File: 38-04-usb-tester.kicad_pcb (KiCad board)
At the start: 2 copper layers, 90 x 90 mm, 68 parts, among them J1 Conn_1x05, J2 USB_C_12401832E402A, J3 USB_C_12401832E402A, J4 USB_Micro-B_KH-MICRO5P-JN, J5 USB_Mini-B_U-M-M5DD-W-1, J6 USB3_A_HC-USB3.0-L168-WP, SW1 SW_DPDT_x2, SW2 ZX-1.27BM-4PSMD, U1 STM32C031K6Tx

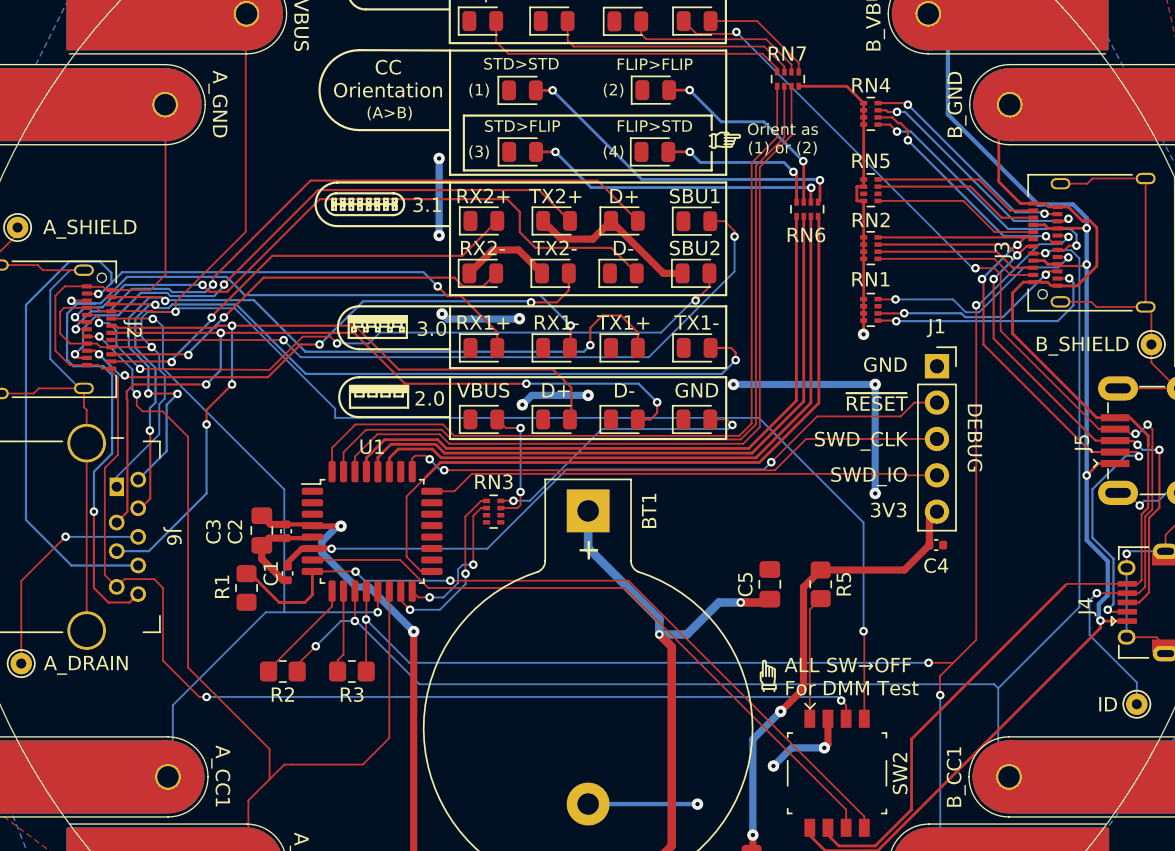
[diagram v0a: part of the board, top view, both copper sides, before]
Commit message: edited schematic, added solder mask expansion, added more thermal reliefs
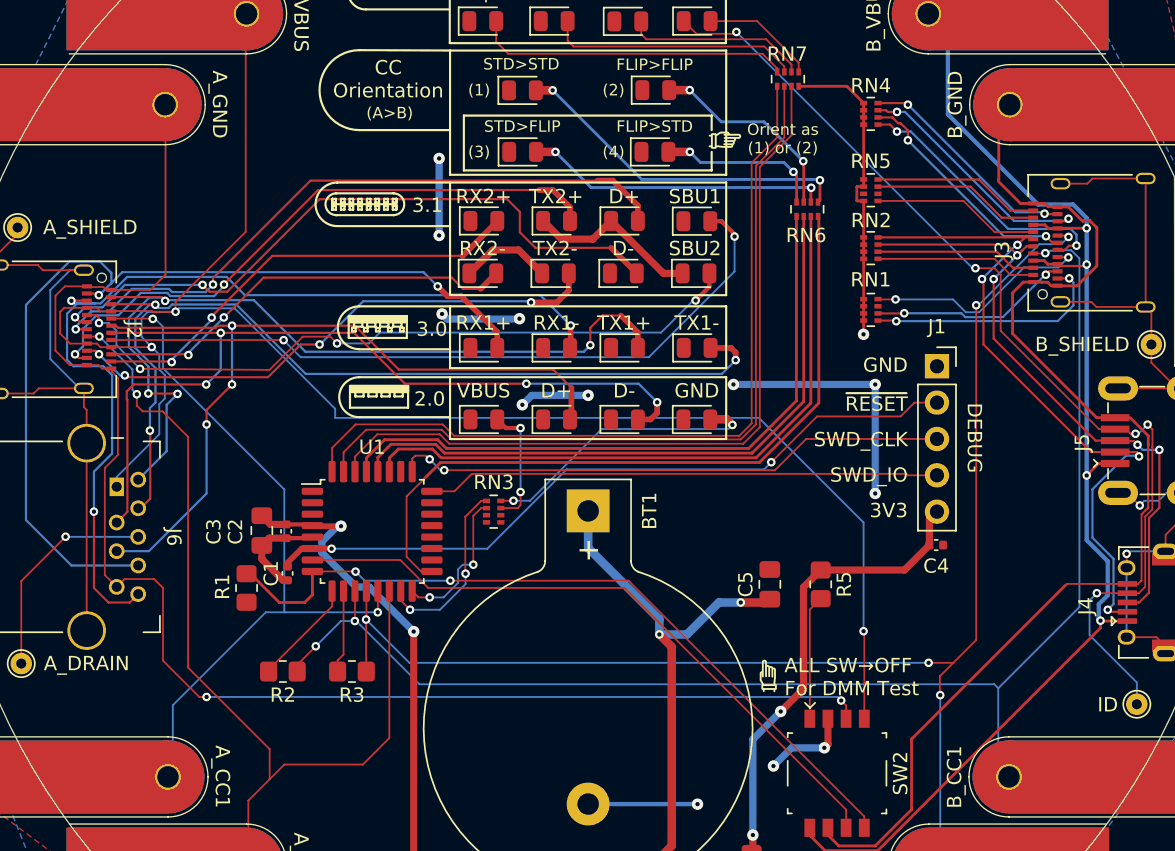
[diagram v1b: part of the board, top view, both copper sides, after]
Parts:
- U1: value STM32C031K6Tx -> STM32C031K6T6
- renumbered REF** to ?
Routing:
- net /A_D2+: track 46.1 -> 46.7 mm
- net /A_SSTx2+: track 42.1 -> 42.7 mm
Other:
- rule pad_to_mask_clearance: 0 -> 0.038
- rule solder_mask_min_width: 0.12 -> 0.1

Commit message: rev 1 sent for prod
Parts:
- R4: value 1K -> 2K
- RN1, RN2, RN3, RN4, RN5, RN6, RN7: value 1K -> 1K6
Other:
- board text added: "Do NOT plug into an external USB port"
- board text added: "ON"
- board text added: "USB Sleuth Rev 1"
- board text removed: "TODO - LOGO"
- board text removed: "USB Sleuth v0.1"

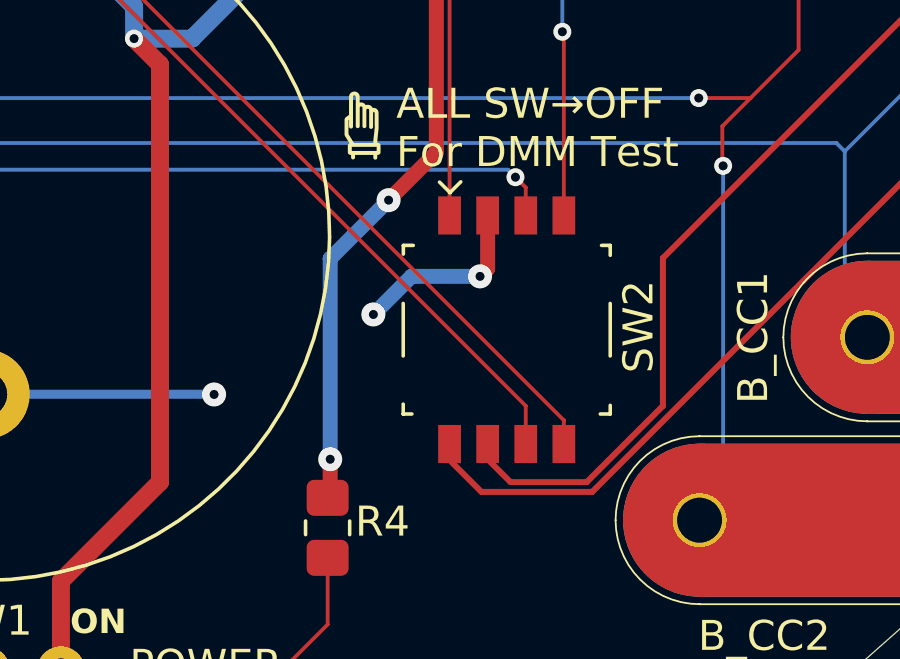
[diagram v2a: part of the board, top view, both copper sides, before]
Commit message: correct SW2 footprint and symbol pin numbering
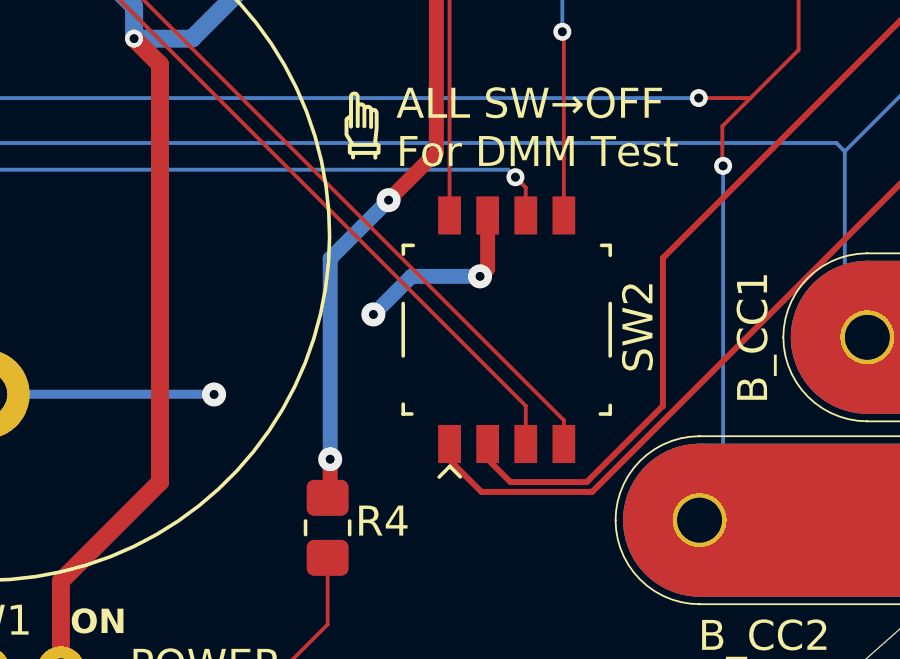
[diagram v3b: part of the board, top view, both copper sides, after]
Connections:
- SW2 pad 2: /B_VBUS_A4 -> GND
- SW2 pad 3: GND -> /A_GND
- SW2 pad 4: /B_GND_A1 -> /A_VBUS
- SW2 pad 5: /A_GND -> /A_VBUS_SENS
- SW2 pad 7: /A_VBUS -> /B_GND_A1
- SW2 pad 8: /A_VBUS_SENS -> /B_VBUS_A4
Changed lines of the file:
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@@
     (pcbplotparams
       (layerselection 0x00010fc_ffffffff)
-      (plot_on_all_layers_selection 0x0000000_00000000)
+      (plot_on_all_layers_selection 0x0001000_00000000)
       (disableapertmacros false)
       (usegerberextensions false)
@@
       (outputformat 1)
       (mirror false)
-      (drillshape 1)
+      (drillshape 0)
       (scaleselection 1)
-      (outputdirectory "")
+      (outputdirectory "production/")
     )
   )
@@
     (fp_line (start -3.115 -2.81) (end -3.445 -2.81)
       (stroke (width 0.12) (type default)) (layer "F.SilkS"))
-    (fp_line (start -1.89 -4.57) (end -2.24 -4.92)
+    (fp_line (start -1.895 4.555) (end -2.250363 4.910363)
       (stroke (width 0.12) (type default)) (layer "F.SilkS"))
-    (fp_line (start -1.89 -4.57) (end -1.53 -4.93)
+    (fp_line (start -1.895 4.555) (end -1.545 4.905)
       (stroke (width 0.12) (type default)) (layer "F.SilkS"))
     (fp_line (start 3.12 2.81) (end 3.45 2.81)
@@
     (pad "1" smd rect (at -1.905 -3.81) (size 0.76 1.27) (layers "F.Cu" "F.Paste" "F.Mask")
       (net 75 "Net-(R5-Pad2)") (pintype "passive") (thermal_bridge_angle 45))
-    (pad "2" smd rect (at -1.905 3.81) (size 0.76 1.27) (layers "F.Cu" "F.Paste" "F.Mask")
-      (net 24 "/B_VBUS_A4") (pintype "passive") (thermal_bridge_angle 45))
-    (pad "3" smd rect (at -0.635 -3.81) (size 0.76 1.27) (layers "F.Cu" "F.Paste" "F.Mask")
+    (pad "2" smd rect (at -0.635 -3.81) (size 0.76 1.27) (layers "F.Cu" "F.Paste" "F.Mask")
       (net 2 "GND") (pintype "passive") (thermal_bridge_angle 45))
-    (pad "4" smd rect (at -0.635 3.81) (size 0.76 1.27) (layers "F.Cu" "F.Paste" "F.Mask")
-      (net 74 "/B_GND_A1") (pintype "passive") (thermal_bridge_angle 45))
-    (pad "5" smd rect (at 0.635 -3.81) (size 0.76 1.27) (layers "F.Cu" "F.Paste" "F.Mask")
+    (pad "3" smd rect (at 0.635 -3.81) (size 0.76 1.27) (layers "F.Cu" "F.Paste" "F.Mask")
       (net 21 "/A_GND") (pintype "passive") (thermal_bridge_angle 45))
-    (pad "6" smd rect (at 0.635 3.81) (size 0.76 1.27) (layers "F.Cu" "F.Paste" "F.Mask")
-      (net 32 "/A_GND_SENS") (pintype "passive") (thermal_bridge_angle 45))
-    (pad "7" smd rect (at 1.905 -3.81) (size 0.76 1.27) (layers "F.Cu" "F.Paste" "F.Mask")
+    (pad "4" smd rect (at 1.905 -3.81) (size 0.76 1.27) (layers "F.Cu" "F.Paste" "F.Mask")
       (net 20 "/A_VBUS") (pintype "passive") (thermal_bridge_angle 45))
-    (pad "8" smd rect (at 1.905 3.81) (size 0.76 1.27) (layers "F.Cu" "F.Paste" "F.Mask")
+    (pad "5" smd rect (at 1.905 3.81) (size 0.76 1.27) (layers "F.Cu" "F.Paste" "F.Mask")
       (net 33 "/A_VBUS_SENS") (pintype "passive") (thermal_bridge_angle 45))
+    (pad "6" smd rect (at 0.635 3.81) (size 0.76 1.27) (layers "F.Cu" "F.Paste" "F.Mask")
+      (net 32 "/A_GND_SENS") (pintype "passive") (thermal_bridge_angle 45))
+    (pad "7" smd rect (at -0.635 3.81) (size 0.76 1.27) (layers "F.Cu" "F.Paste" "F.Mask")
+      (net 74 "/B_GND_A1") (pintype "passive") (thermal_bridge_angle 45))
+    (pad "8" smd rect (at -1.905 3.81) (size 0.76 1.27) (layers "F.Cu" "F.Paste" "F.Mask")
+      (net 24 "/B_VBUS_A4") (pintype "passive") (thermal_bridge_angle 45))
   )
   (footprint "Capacitor_SMD:C_0805_2012Metric_Pad1.18x1.45mm_HandSolder" (layer "F.Cu")
